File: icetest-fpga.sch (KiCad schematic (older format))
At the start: 20 parts, among them J1 R, J2 R, J3 R

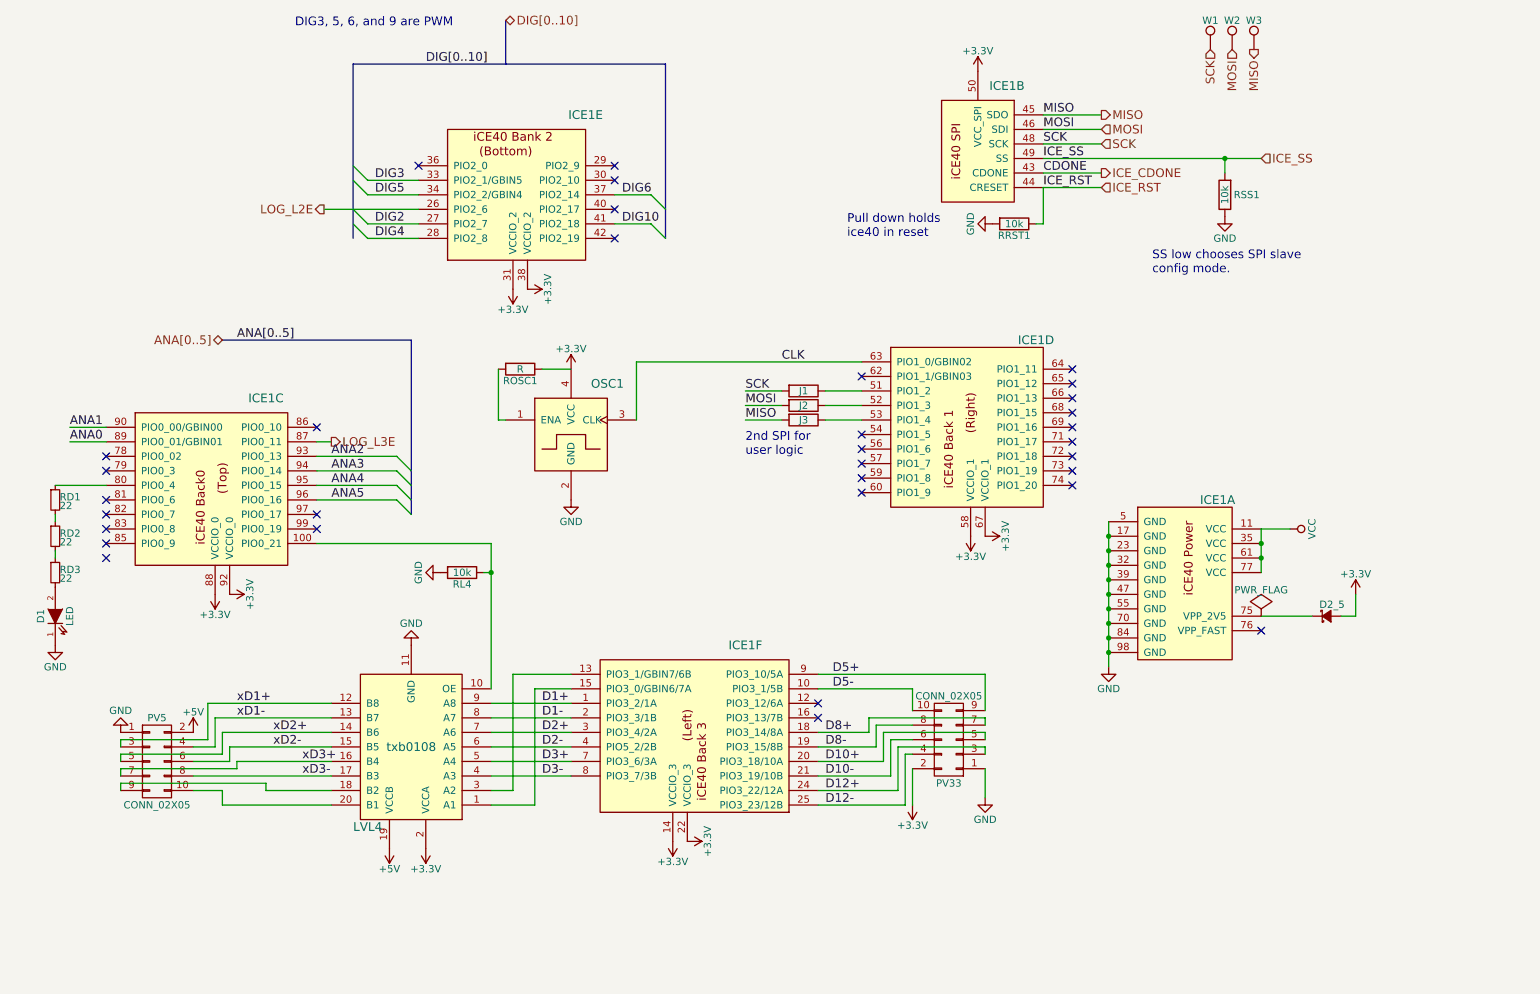
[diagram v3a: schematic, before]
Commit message: fix schematic bugs
signal on N/C pin on ice40
1.2V regulator R divider moved to input side
Remove R divider for 3.3V (not needed for fixed V model)
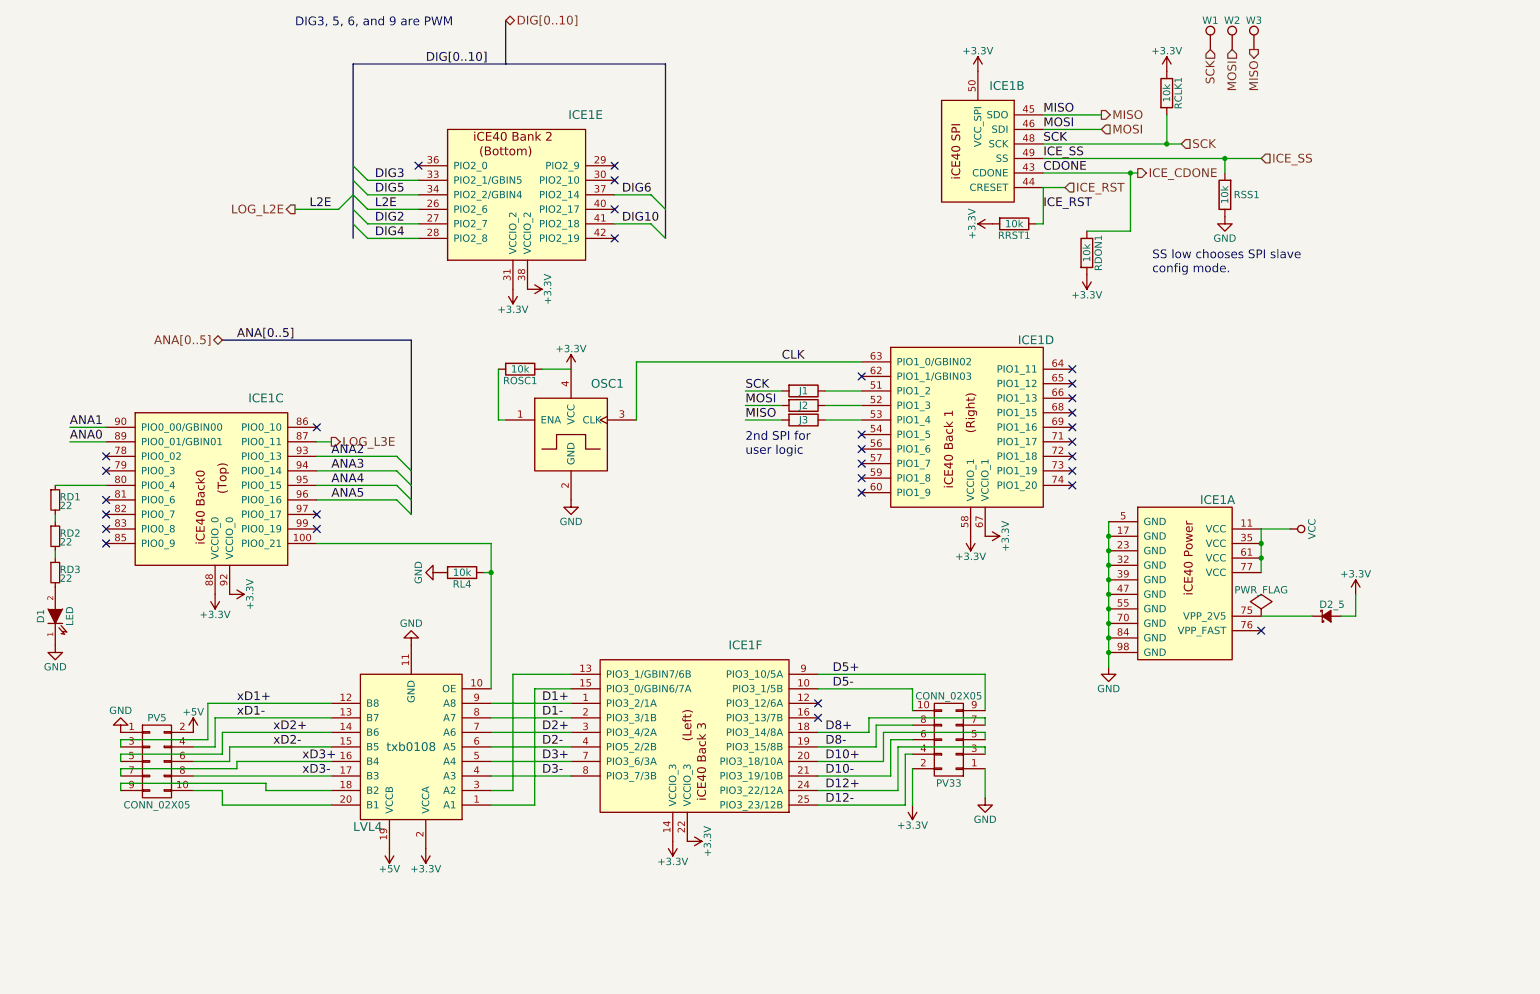
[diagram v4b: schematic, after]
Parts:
- added RCLK1, RDON1: 10k, Resistors_SMD:R_0603_HandSoldering, symbol R
- ROSC1: value R -> 10k
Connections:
- net +3V3: now also RRST1.2, RCLK1.1, RDON1.2
- net GND: no longer RRST1.2
- net ICE_CDONE: now also RDON1.1
- net SCK: now also RCLK1.2
- no-connect marks 33 -> 32
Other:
- note removed: "Pull down holds\nice40 in reset"
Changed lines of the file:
@@
 $EndDescr
 $Comp
-L VCC #PWR050
+L VCC #PWR049
 U 1 1 578C4CE2
 P 9350 4400
-F 0 "#PWR050" H 9350 4250 50  0001 C CNN
+F 0 "#PWR049" H 9350 4250 50  0001 C CNN
 F 1 "VCC" H 9350 4550 50  0000 C CNN
 F 2 "" H 9350 4400 50  0000 C CNN
@@
 $EndComp
 $Comp
-L GND #PWR051
+L GND #PWR050
 U 1 1 578C4D81
 P 8100 5350
-F 0 "#PWR051" H 8100 5100 50  0001 C CNN
+F 0 "#PWR050" H 8100 5100 50  0001 C CNN
 F 1 "GND" H 8100 5200 50  0000 C CNN
 F 2 "" H 8100 5350 50  0000 C CNN
@@
 $EndComp
 $Comp
-L +3.3V #PWR052
+L +3.3V #PWR051
 U 1 1 578C4F49
 P 9800 4850
-F 0 "#PWR052" H 9800 4700 50  0001 C CNN
+F 0 "#PWR051" H 9800 4700 50  0001 C CNN
 F 1 "+3.3V" H 9800 4990 50  0000 C CNN
 F 2 "" H 9800 4850 50  0000 C CNN
@@
 $EndComp
 $Comp
-L +3.3V #PWR053
+L +3.3V #PWR052
 U 1 1 578C5E12
 P 7200 1250
-F 0 "#PWR053" H 7200 1100 50  0001 C CNN
+F 0 "#PWR052" H 7200 1100 50  0001 C CNN
 F 1 "+3.3V" H 7200 1390 50  0000 C CNN
 F 2 "" H 7200 1250 50  0000 C CNN
@@
 Text Label 7650 1950 0    60   ~ 0
 CDONE
-Text Label 7650 2050 0    60   ~ 0
+Text Label 7650 2200 0    60   ~ 0
 ICE_RST
 $Comp
@@
 $EndComp
 $Comp
-L GND #PWR054
-U 1 1 578C65C7
-P 7300 2300
-F 0 "#PWR054" H 7300 2050 50  0001 C CNN
-F 1 "GND" H 7300 2150 50  0000 C CNN
-F 2 "" H 7300 2300 50  0000 C CNN
-F 3 "" H 7300 2300 50  0000 C CNN
-	1    7300 2300
-	0    1    1    0
-$EndComp
-Text Notes 6300 2400 0    60   ~ 0
-Pull down holds\nice40 in reset
-$Comp
-L PWR_FLAG #FLG055
+L PWR_FLAG #FLG053
 U 1 1 578C6B04
 P 9150 5000
-F 0 "#FLG055" H 9150 5095 50  0001 C CNN
+F 0 "#FLG053" H 9150 5095 50  0001 C CNN
 F 1 "PWR_FLAG" H 9150 5180 50  0000 C CNN
 F 2 "" H 9150 5000 50  0000 C CNN
@@
 Text HLabel 8050 1650 2    60   Input ~ 0
 MOSI
-Text HLabel 8050 1750 2    60   Input ~ 0
+Text HLabel 8600 1750 2    60   Input ~ 0
 SCK
 Text HLabel 9150 1850 2    60   Input ~ 0
 ICE_SS
-Text HLabel 8050 1950 2    60   Output ~ 0
+Text HLabel 8300 1950 2    60   Output ~ 0
 ICE_CDONE
-Text HLabel 8050 2050 2    60   Input ~ 0
+Text HLabel 7800 2050 2    60   Input ~ 0
 ICE_RST
 $Comp
@@
 DIG10
 $Comp
-L +3.3V #PWR056
+L +3.3V #PWR054
 U 1 1 578D33A2
 P 4000 2750
-F 0 "#PWR056" H 4000 2600 50  0001 C CNN
+F 0 "#PWR054" H 4000 2600 50  0001 C CNN
 F 1 "+3.3V" H 4000 2890 50  0000 C CNN
 F 2 "" H 4000 2750 50  0000 C CNN
@@
 $EndComp
 $Comp
-L +3.3V #PWR057
+L +3.3V #PWR055
 U 1 1 578D33C6
 P 4100 2750
-F 0 "#PWR057" H 4100 2600 50  0001 C CNN
+F 0 "#PWR055" H 4100 2600 50  0001 C CNN
 F 1 "+3.3V" H 4100 2890 50  0000 C CNN
 F 2 "" H 4100 2750 50  0000 C CNN
@@
 	0    1    1    0
 $EndComp
-Text HLabel 2700 2200 0    60   Output ~ 0
+Text HLabel 2500 2200 0    60   Output ~ 0
 LOG_L2E
 Text HLabel 2750 3800 2    60   Output ~ 0
@@
 ANA5
 $Comp
-L +3.3V #PWR058
+L +3.3V #PWR056
 U 1 1 578D500A
 P 2050 4850
-F 0 "#PWR058" H 2050 4700 50  0001 C CNN
+F 0 "#PWR056" H 2050 4700 50  0001 C CNN
 F 1 "+3.3V" H 2050 4990 50  0000 C CNN
 F 2 "" H 2050 4850 50  0000 C CNN
@@
 $EndComp
 $Comp
-L +3.3V #PWR059
+L +3.3V #PWR057
 U 1 1 578D5027
 P 1950 4850
-F 0 "#PWR059" H 1950 4700 50  0001 C CNN
+F 0 "#PWR057" H 1950 4700 50  0001 C CNN
 F 1 "+3.3V" H 1950 4990 50  0000 C CNN
 F 2 "" H 1950 4850 50  0000 C CNN
@@
 $EndComp
 $Comp
-L +3.3V #PWR060
+L +3.3V #PWR058
 U 1 1 578BAE99
 P 4400 3300
-F 0 "#PWR060" H 4400 3150 50  0001 C CNN
+F 0 "#PWR058" H 4400 3150 50  0001 C CNN
 F 1 "+3.3V" H 4400 3440 50  0000 C CNN
 F 2 "" H 4400 3300 50  0000 C CNN
@@
 P 4050 3300
 F 0 "ROSC1" V 4130 3300 50  0000 C CNN
-F 1 "R" V 4050 3300 50  0000 C CNN
+F 1 "10k" V 4050 3300 50  0000 C CNN
 F 2 "Resistors_SMD:R_0603_HandSoldering" V 3980 3300 50  0001 C CNN
 F 3 "" H 4050 3300 50  0000 C CNN
@@
 $EndComp
 $Comp
-L GND #PWR061
+L GND #PWR059
 U 1 1 578BB26B
 P 4400 4200
-F 0 "#PWR061" H 4400 3950 50  0001 C CNN
+F 0 "#PWR059" H 4400 3950 50  0001 C CNN
 F 1 "GND" H 4400 4050 50  0000 C CNN
 F 2 "" H 4400 4200 50  0000 C CNN
@@
 $EndComp
 $Comp
-L +3.3V #PWR062
+L +3.3V #PWR060
 U 1 1 578BBA24
 P 5100 6550
-F 0 "#PWR062" H 5100 6400 50  0001 C CNN
+F 0 "#PWR060" H 5100 6400 50  0001 C CNN
 F 1 "+3.3V" H 5100 6690 50  0000 C CNN
 F 2 "" H 5100 6550 50  0000 C CNN
@@
 $EndComp
 $Comp
-L +3.3V #PWR063
+L +3.3V #PWR061
 U 1 1 578BBA7C
 P 5200 6550
-F 0 "#PWR063" H 5200 6400 50  0001 C CNN
+F 0 "#PWR061" H 5200 6400 50  0001 C CNN
 F 1 "+3.3V" H 5200 6690 50  0000 C CNN
 F 2 "" H 5200 6550 50  0000 C CNN
@@
 $EndComp
 $Comp
-L +3.3V #PWR064
+L +3.3V #PWR062
 U 1 1 578BBABE
 P 7250 4450
-F 0 "#PWR064" H 7250 4300 50  0001 C CNN
+F 0 "#PWR062" H 7250 4300 50  0001 C CNN
 F 1 "+3.3V" H 7250 4590 50  0000 C CNN
 F 2 "" H 7250 4450 50  0000 C CNN
@@
 $EndComp
 $Comp
-L +3.3V #PWR065
+L +3.3V #PWR063
 U 1 1 578BBAEA
 P 7150 4450
-F 0 "#PWR065" H 7150 4300 50  0001 C CNN
+F 0 "#PWR063" H 7150 4300 50  0001 C CNN
 F 1 "+3.3V" H 7150 4590 50  0000 C CNN
 F 2 "" H 7150 4450 50  0000 C CNN
@@
 $EndComp
 $Comp
-L GND #PWR066
+L GND #PWR064
 U 1 1 578BC0E8
 P 3500 4700
-F 0 "#PWR066" H 3500 4450 50  0001 C CNN
+F 0 "#PWR064" H 3500 4450 50  0001 C CNN
 F 1 "GND" H 3500 4550 50  0000 C CNN
 F 2 "" H 3500 4700 50  0000 C CNN
@@
 $EndComp
 $Comp
-L +5V #PWR067
+L +5V #PWR065
 U 1 1 578BC3E1
 P 1800 5800
-F 0 "#PWR067" H 1800 5650 50  0001 C CNN
+F 0 "#PWR065" H 1800 5650 50  0001 C CNN
 F 1 "+5V" H 1800 5940 50  0000 C CNN
 F 2 "" H 1800 5800 50  0000 C CNN
@@
 $EndComp
 $Comp
-L GND #PWR068
+L GND #PWR066
 U 1 1 578BC4AA
 P 3300 5200
-F 0 "#PWR068" H 3300 4950 50  0001 C CNN
+F 0 "#PWR066" H 3300 4950 50  0001 C CNN
 F 1 "GND" H 3300 5050 50  0000 C CNN
 F 2 "" H 3300 5200 50  0000 C CNN
@@
 $EndComp
 $Comp
-L +3.3V #PWR069
+L +3.3V #PWR067
 U 1 1 578BC509
 P 3400 6600
-F 0 "#PWR069" H 3400 6450 50  0001 C CNN
+F 0 "#PWR067" H 3400 6450 50  0001 C CNN
 F 1 "+3.3V" H 3400 6740 50  0000 C CNN
 F 2 "" H 3400 6600 50  0000 C CNN
@@
 $EndComp
 $Comp
-L +5V #PWR070
+L +5V #PWR068
 U 1 1 578BC5B8
 P 3150 6600
-F 0 "#PWR070" H 3150 6450 50  0001 C CNN
+F 0 "#PWR068" H 3150 6450 50  0001 C CNN
 F 1 "+5V" H 3150 6740 50  0000 C CNN
 F 2 "" H 3150 6600 50  0000 C CNN
@@
 $EndComp
 $Comp
-L GND #PWR071
+L GND #PWR069
 U 1 1 578BD4EA
 P 1300 5800
-F 0 "#PWR071" H 1300 5550 50  0001 C CNN
+F 0 "#PWR069" H 1300 5550 50  0001 C CNN
 F 1 "GND" H 1300 5650 50  0000 C CNN
 F 2 "" H 1300 5800 50  0000 C CNN
@@
 $EndComp
 $Comp
-L GND #PWR072
+L GND #PWR070
 U 1 1 578BD754
 P 7250 6250
-F 0 "#PWR072" H 7250 6000 50  0001 C CNN
+F 0 "#PWR070" H 7250 6000 50  0001 C CNN
 F 1 "GND" H 7250 6100 50  0000 C CNN
 F 2 "" H 7250 6250 50  0000 C CNN
@@
 $EndComp
 $Comp
-L +3.3V #PWR073
+L +3.3V #PWR071
 U 1 1 578BD789
 P 6750 6300
-F 0 "#PWR073" H 6750 6150 50  0001 C CNN
+F 0 "#PWR071" H 6750 6150 50  0001 C CNN
 F 1 "+3.3V" H 6750 6440 50  0000 C CNN
 F 2 "" H 6750 6300 50  0000 C CNN
@@
 	8050 1650 7650 1650
 Wire Wire Line
-	7650 1750 8050 1750
+	7650 1750 8600 1750
 Wire Wire Line
 	7650 1850 9150 1850
 Wire Wire Line
-	7650 1950 8050 1950
-Wire Wire Line
-	8050 2050 7650 2050
+	7650 1950 8300 1950
+Wire Wire Line
+	7800 2050 7650 2050
 Wire Wire Line
 	7650 2050 7650 2300
@@
 Wire Bus Line
 	2000 3100 3300 3100
-Wire Wire Line
-	2700 2200 3350 2200
 Wire Wire Line
 	3200 4200 2650 4200
@@
 NoConn ~ 1200 4300
 NoConn ~ 1200 4500
-NoConn ~ 1200 4600
 Text Label 6200 5400 0    60   ~ 0
 D5+
@@
 $EndComp
 $Comp
-L GND #PWR074
+L GND #PWR072
 U 1 1 578DB32E
 P 850 5200
-F 0 "#PWR074" H 850 4950 50  0001 C CNN
+F 0 "#PWR072" H 850 4950 50  0001 C CNN
 F 1 "GND" H 850 5050 50  0000 C CNN
 F 2 "" H 850 5200 50  0000 C CNN
@@
 $EndComp
 $Comp
-L GND #PWR075
+L GND #PWR073
 U 1 1 5793BE07
 P 8900 2250
-F 0 "#PWR075" H 8900 2000 50  0001 C CNN
+F 0 "#PWR073" H 8900 2000 50  0001 C CNN
 F 1 "GND" H 8900 2100 50  0000 C CNN
 F 2 "" H 8900 2250 50  0000 C CNN
@@
 Wire Wire Line
 	5850 3650 5600 3650
+$Comp
+L +3.3V #PWR074
+U 1 1 57A69258
+P 7300 2300
+F 0 "#PWR074" H 7300 2150 50  0001 C CNN
+F 1 "+3.3V" H 7300 2440 50  0000 C CNN
+F 2 "" H 7300 2300 50  0000 C CNN
+F 3 "" H 7300 2300 50  0000 C CNN
+	1    7300 2300
+	0    -1   -1   0
+$EndComp
+$Comp
+L R RDON1
+U 1 1 57A694A2
+P 7950 2500
+F 0 "RDON1" V 8030 2500 50  0000 C CNN
+F 1 "10k" V 7950 2500 50  0000 C CNN
+F 2 "Resistors_SMD:R_0603_HandSoldering" V 7880 2500 50  0001 C CNN
+F 3 "" H 7950 2500 50  0000 C CNN
+	1    7950 2500
+	1    0    0    -1
+$EndComp
+$Comp
+L +3.3V #PWR075
+U 1 1 57A694A8
+P 7950 2650
+F 0 "#PWR075" H 7950 2500 50  0001 C CNN
+F 1 "+3.3V" H 7950 2790 50  0000 C CNN
+F 2 "" H 7950 2650 50  0000 C CNN
+F 3 "" H 7950 2650 50  0000 C CNN
+	1    7950 2650
+	-1   0    0    1
+$EndComp
+Wire Wire Line
+	8250 1950 8250 2350
+Wire Wire Line
+	8250 2350 7950 2350
+Connection ~ 8250 1950
+$Comp
+L R RCLK1
+U 1 1 57A6985B
+P 8500 1400
+F 0 "RCLK1" V 8580 1400 50  0000 C CNN
+F 1 "10k" V 8500 1400 50  0000 C CNN
+F 2 "Resistors_SMD:R_0603_HandSoldering" V 8430 1400 50  0001 C CNN
+F 3 "" H 8500 1400 50  0000 C CNN
+	1    8500 1400
+	1    0    0    -1
+$EndComp
+$Comp
+L +3.3V #PWR076
+U 1 1 57A698FC
+P 8500 1250
+F 0 "#PWR076" H 8500 1100 50  0001 C CNN
+F 1 "+3.3V" H 8500 1390 50  0000 C CNN
+F 2 "" H 8500 1250 50  0000 C CNN
+F 3 "" H 8500 1250 50  0000 C CNN
+	1    8500 1250
+	1    0    0    -1
+$EndComp
+Wire Wire Line
+	8500 1550 8500 1750
+Connection ~ 8500 1750
+Entry Wire Line
+	2900 2100 3000 2200
+Entry Wire Line
+	2800 2200 2900 2100
+Wire Wire Line
+	3350 2200 3000 2200
+Wire Wire Line
+	2800 2200 2500 2200
+Text Label 3050 2200 0    60   ~ 0
+L2E
+Text Label 2600 2200 0    60   ~ 0
+L2E
 $EndSCHEMATC

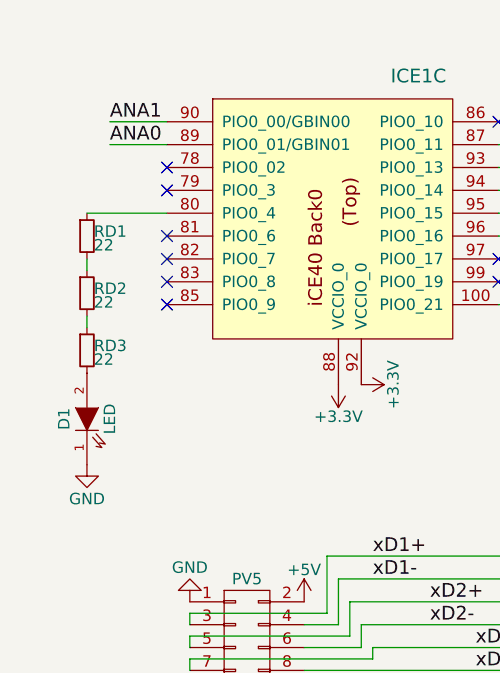
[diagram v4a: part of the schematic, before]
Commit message: add LED2 and update layout
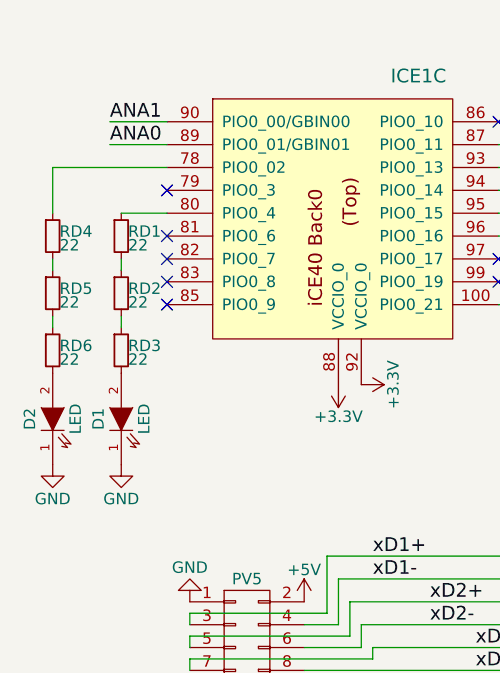
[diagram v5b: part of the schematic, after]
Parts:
- added D2: LED, local:D_0603_HandSoldering, symbol LED
- added RD4, RD5, RD6: 22, Resistors_SMD:R_0603_HandSoldering, symbol R_Small
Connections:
- net GND: now also D2.1 (K)
- net at ICE1.78 (PIO0_02): now also RD4.1
- new net: D2.2 (A), RD6.2
- new net: RD4.2, RD5.1
- new net: RD5.2, RD6.1
- no-connect marks 32 -> 31
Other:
- moved on the sheet: D1, RD1, RD2, RD3
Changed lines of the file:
@@
 	1200 3800 950  3800
 NoConn ~ 2650 3700
-NoConn ~ 1200 3900
 Wire Wire Line
 	4700 2300 4950 2300
@@
 L LED D1
 U 1 1 578DAD29
-P 850 5000
-F 0 "D1" H 850 5100 50  0000 C CNN
-F 1 "LED" H 850 4900 50  0000 C CNN
-F 2 "local:D_0603_HandSoldering" H 850 5000 50  0001 C CNN
-F 3 "" H 850 5000 50  0000 C CNN
-	1    850  5000
+P 1000 5000
+F 0 "D1" H 1000 5100 50  0000 C CNN
+F 1 "LED" H 1000 4900 50  0000 C CNN
+F 2 "local:D_0603_HandSoldering" H 1000 5000 50  0001 C CNN
+F 3 "" H 1000 5000 50  0000 C CNN
+	1    1000 5000
 	0    -1   -1   0
 $EndComp
@@
 L GND #PWR072
 U 1 1 578DB32E
-P 850 5200
-F 0 "#PWR072" H 850 4950 50  0001 C CNN
-F 1 "GND" H 850 5050 50  0000 C CNN
-F 2 "" H 850 5200 50  0000 C CNN
-F 3 "" H 850 5200 50  0000 C CNN
-	1    850  5200
-	1    0    0    -1
-$EndComp
-Wire Wire Line
-	1200 4100 850  4100
-Wire Wire Line
-	850  4600 850  4550
-Wire Wire Line
-	850  4350 850  4300
+P 1000 5200
+F 0 "#PWR072" H 1000 4950 50  0001 C CNN
+F 1 "GND" H 1000 5050 50  0000 C CNN
+F 2 "" H 1000 5200 50  0000 C CNN
+F 3 "" H 1000 5200 50  0000 C CNN
+	1    1000 5200
+	1    0    0    -1
+$EndComp
+Wire Wire Line
+	1200 4100 1000 4100
+Wire Wire Line
+	1000 4600 1000 4550
+Wire Wire Line
+	1000 4350 1000 4300
 $Comp
 L R_Small RD2
 U 1 1 578DAF76
-P 850 4450
-F 0 "RD2" H 880 4470 50  0000 L CNN
-F 1 "22" H 880 4410 50  0000 L CNN
-F 2 "Resistors_SMD:R_0603_HandSoldering" H 850 4450 50  0001 C CNN
-F 3 "" H 850 4450 50  0000 C CNN
-	1    850  4450
+P 1000 4450
+F 0 "RD2" H 1030 4470 50  0000 L CNN
+F 1 "22" H 1030 4410 50  0000 L CNN
+F 2 "Resistors_SMD:R_0603_HandSoldering" H 1000 4450 50  0001 C CNN
+F 3 "" H 1000 4450 50  0000 C CNN
+	1    1000 4450
 	1    0    0    -1
 $EndComp
@@
 L R_Small RD3
 U 1 1 578DAFC3
-P 850 4700
-F 0 "RD3" H 880 4720 50  0000 L CNN
-F 1 "22" H 880 4660 50  0000 L CNN
-F 2 "Resistors_SMD:R_0603_HandSoldering" H 850 4700 50  0001 C CNN
-F 3 "" H 850 4700 50  0000 C CNN
-	1    850  4700
+P 1000 4700
+F 0 "RD3" H 1030 4720 50  0000 L CNN
+F 1 "22" H 1030 4660 50  0000 L CNN
+F 2 "Resistors_SMD:R_0603_HandSoldering" H 1000 4700 50  0001 C CNN
+F 3 "" H 1000 4700 50  0000 C CNN
+	1    1000 4700
 	1    0    0    -1
 $EndComp
@@
 L R_Small RD1
 U 1 1 578DAE6A
-P 850 4200
-F 0 "RD1" H 880 4220 50  0000 L CNN
-F 1 "22" H 880 4160 50  0000 L CNN
-F 2 "Resistors_SMD:R_0603_HandSoldering" H 850 4200 50  0001 C CNN
-F 3 "" H 850 4200 50  0000 C CNN
-	1    850  4200
+P 1000 4200
+F 0 "RD1" H 1030 4220 50  0000 L CNN
+F 1 "22" H 1030 4160 50  0000 L CNN
+F 2 "Resistors_SMD:R_0603_HandSoldering" H 1000 4200 50  0001 C CNN
+F 3 "" H 1000 4200 50  0000 C CNN
+	1    1000 4200
 	1    0    0    -1
 $EndComp
@@
 Text Label 2600 2200 0    60   ~ 0
 L2E
+$Comp
+L LED D2
+U 1 1 57A71419
+P 700 5000
+F 0 "D2" H 700 5100 50  0000 C CNN
+F 1 "LED" H 700 4900 50  0000 C CNN
+F 2 "local:D_0603_HandSoldering" H 700 5000 50  0001 C CNN
+F 3 "" H 700 5000 50  0000 C CNN
+	1    700  5000
+	0    -1   -1   0
+$EndComp
+$Comp
+L GND #PWR?
+U 1 1 57A7141F
+P 700 5200
+F 0 "#PWR?" H 700 4950 50  0001 C CNN
+F 1 "GND" H 700 5050 50  0000 C CNN
+F 2 "" H 700 5200 50  0000 C CNN
+F 3 "" H 700 5200 50  0000 C CNN
+	1    700  5200
+	1    0    0    -1
+$EndComp
+Wire Wire Line
+	700  4600 700  4550
+Wire Wire Line
+	700  4350 700  4300
+$Comp
+L R_Small RD5
+U 1 1 57A71427
+P 700 4450
+F 0 "RD5" H 730 4470 50  0000 L CNN
+F 1 "22" H 730 4410 50  0000 L CNN
+F 2 "Resistors_SMD:R_0603_HandSoldering" H 700 4450 50  0001 C CNN
+F 3 "" H 700 4450 50  0000 C CNN
+	1    700  4450
+	1    0    0    -1
+$EndComp
+$Comp
+L R_Small RD6
+U 1 1 57A7142D
+P 700 4700
+F 0 "RD6" H 730 4720 50  0000 L CNN
+F 1 "22" H 730 4660 50  0000 L CNN
+F 2 "Resistors_SMD:R_0603_HandSoldering" H 700 4700 50  0001 C CNN
+F 3 "" H 700 4700 50  0000 C CNN
+	1    700  4700
+	1    0    0    -1
+$EndComp
+$Comp
+L R_Small RD4
+U 1 1 57A71433
+P 700 4200
+F 0 "RD4" H 730 4220 50  0000 L CNN
+F 1 "22" H 730 4160 50  0000 L CNN
+F 2 "Resistors_SMD:R_0603_HandSoldering" H 700 4200 50  0001 C CNN
+F 3 "" H 700 4200 50  0000 C CNN
+	1    700  4200
+	1    0    0    -1
+$EndComp
+Wire Wire Line
+	1200 3900 700  3900
+Wire Wire Line
+	700  3900 700  4100
 $EndSCHEMATC

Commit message: clean and oshpart rules
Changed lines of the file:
@@
 Text HLabel 2750 3800 2    60   Output ~ 0
 LOG_L3E
-Text HLabel 2000 3100 0    60   BiDi ~ 0
+Text HLabel 2000 2900 1    60   BiDi ~ 0
 ANA[0..5]
 Text Label 2100 3100 0    60   ~ 0
@@
 Wire Wire Line
 	4700 2100 4950 2100
-Wire Bus Line
-	2000 3100 3300 3100
 Wire Wire Line
 	3200 4200 2650 4200
@@
 Wire Wire Line
 	700  3900 700  4100
+Wire Bus Line
+	2000 2900 2000 3100
+Entry Wire Line
+	850  3600 950  3700
+Entry Wire Line
+	850  3700 950  3800
+Wire Bus Line
+	850  3100 3300 3100
+Wire Bus Line
+	850  3100 850  3700
 $EndSCHEMATC
